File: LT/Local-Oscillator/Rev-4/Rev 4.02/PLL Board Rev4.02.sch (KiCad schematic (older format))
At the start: 69 parts, among them J1 Conn_01x02_Male, J13 Conn_01x02_Male, J14 Conn_01x02_Male, J15 Conn_01x02_Male, J16 Conn_01x02_Male, J17 Conn_01x02_Male, J18 Conn_Coaxial, J2 Conn_Coaxial, J20 Conn_01x02_Male, J3 Conn_Coaxial, J4 Conn_01x04_Male, J5 Conn_01x02_Male, J7 Conn_01x02_Male, J8 Conn_01x02_Male, Q1 2N5486 JFET, Q2 2N5486 JFET, U1 LMX231X, U2 L7808

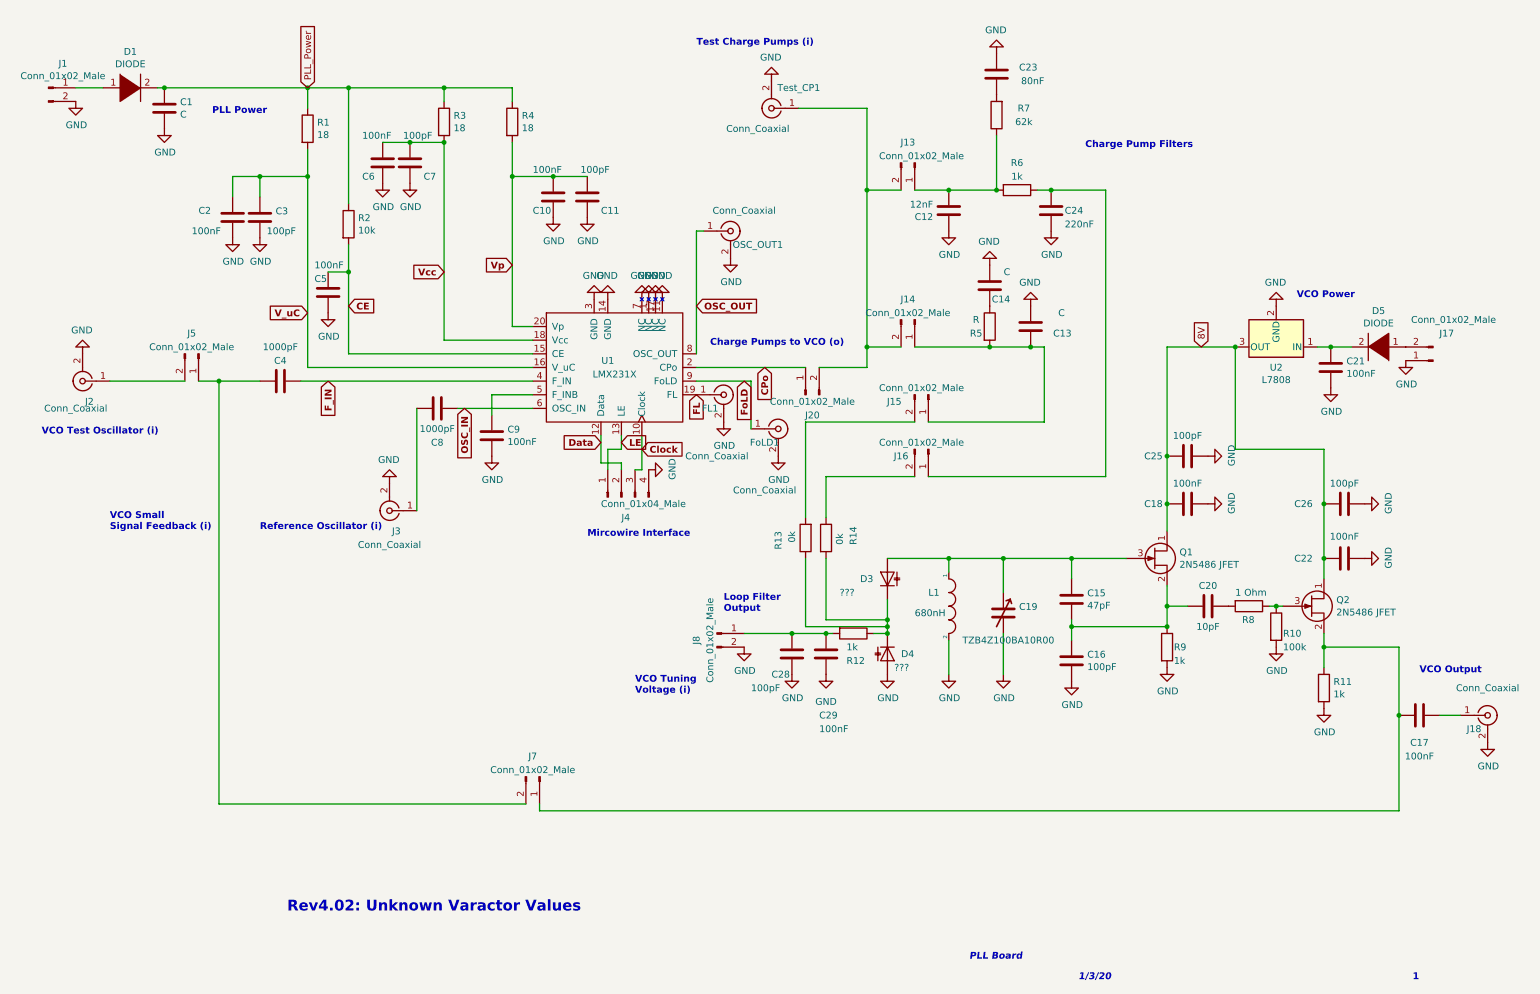
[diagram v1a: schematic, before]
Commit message: Finished PLL Revisions on KiCad
The KiCad files for the PLL have been uploaded to github and the integration to the "Real Resistor" symbol has begun
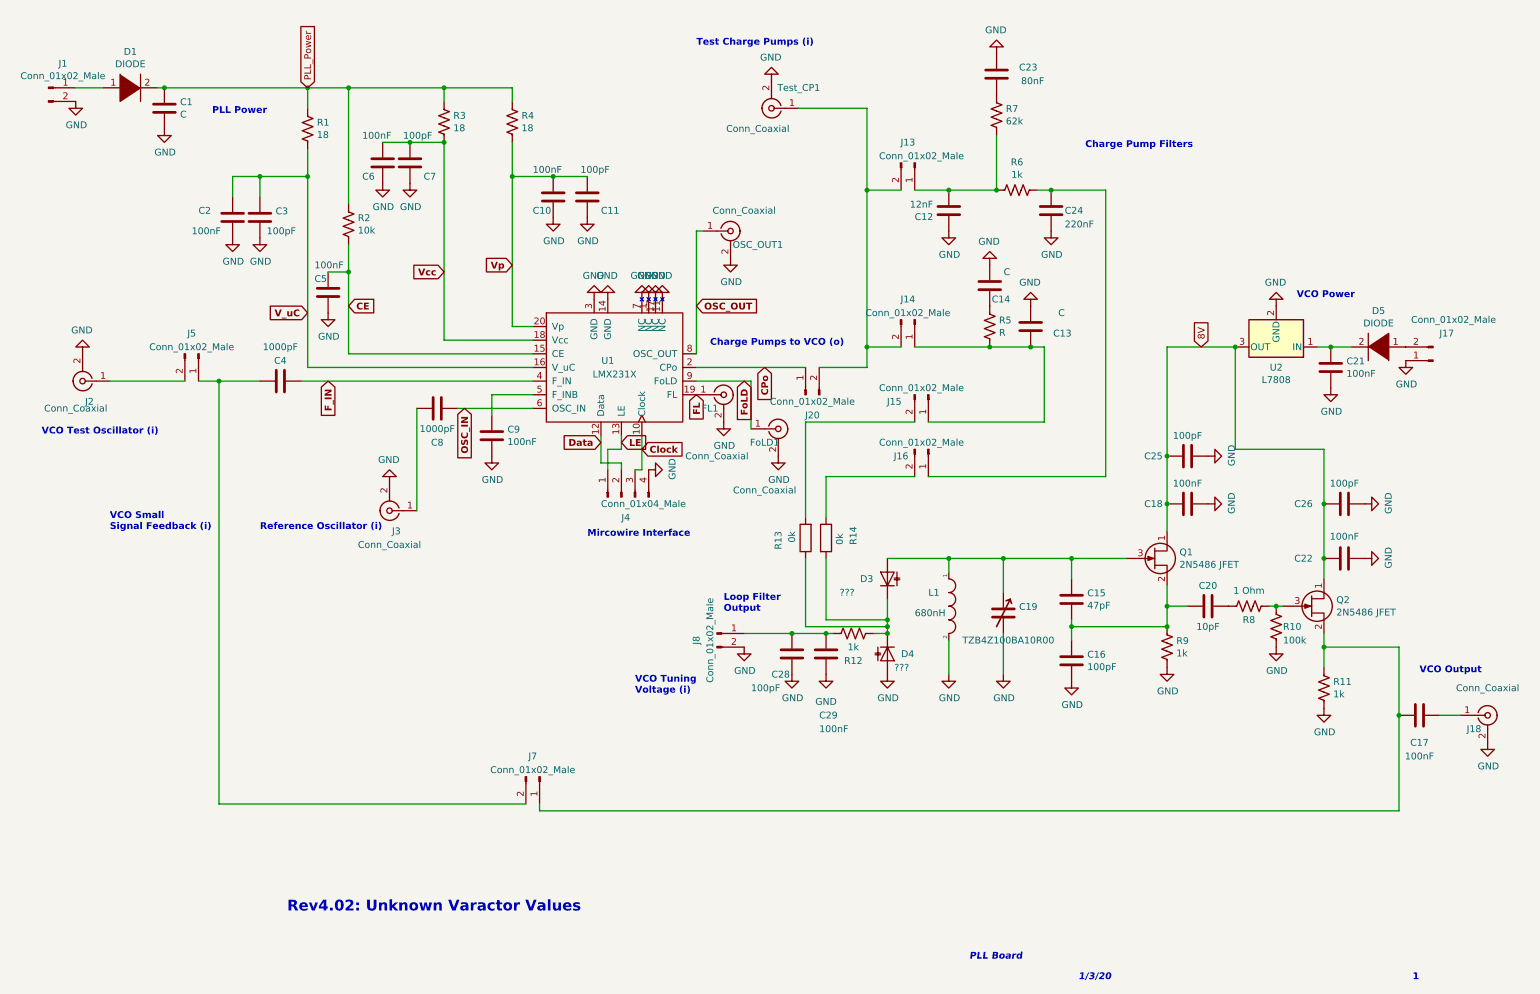
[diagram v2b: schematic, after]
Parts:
- removed R1, R3, R4: 18, Resistor_SMD:R_0805_2012Metric_Pad1.15x1.40mm_HandSolder, symbol PLL-Board-Rev4.02-rescue:R-Device-Complete-PLL-Board-Rev4-rescue-PLL-Board-Rev4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
- removed R10: 100k, Resistor_SMD:R_0805_2012Metric_Pad1.15x1.40mm_HandSolder, symbol PLL-Board-Rev4.02-rescue:R-Device-Complete-PLL-Board-Rev4-rescue-PLL-Board-Rev4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
- removed R11, R12, R6, R9: 1k, Resistor_SMD:R_0805_2012Metric_Pad1.15x1.40mm_HandSolder, symbol PLL-Board-Rev4.02-rescue:R-Device-Complete-PLL-Board-Rev4-rescue-PLL-Board-Rev4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
- removed R2: 10k, Resistor_SMD:R_0805_2012Metric_Pad1.15x1.40mm_HandSolder, symbol PLL-Board-Rev4.02-rescue:R-Device-Complete-PLL-Board-Rev4-rescue-PLL-Board-Rev4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
- removed R5: R, Resistor_SMD:R_0805_2012Metric_Pad1.15x1.40mm_HandSolder, symbol PLL-Board-Rev4.02-rescue:R-Device-Complete-PLL-Board-Rev4-rescue-PLL-Board-Rev4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
- removed R7: 62k, Resistor_SMD:R_0805_2012Metric_Pad1.15x1.40mm_HandSolder, symbol PLL-Board-Rev4.02-rescue:R-Device-Complete-PLL-Board-Rev4-rescue-PLL-Board-Rev4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
- removed R8: 1 Ohm, Resistor_SMD:R_0805_2012Metric_Pad1.15x1.40mm_HandSolder, symbol PLL-Board-Rev4.02-rescue:R-Device-Complete-PLL-Board-Rev4-rescue-PLL-Board-Rev4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
- added R1, R3, R4: 18, Resistor_SMD:R_0805_2012Metric_Pad1.15x1.40mm_HandSolder, symbol Device:R
- added R10: 100k, Resistor_SMD:R_0805_2012Metric_Pad1.15x1.40mm_HandSolder, symbol Device:R
- added R11, R12, R6, R9: 1k, Resistor_SMD:R_0805_2012Metric_Pad1.15x1.40mm_HandSolder, symbol Device:R
- added R2: 10k, Resistor_SMD:R_0805_2012Metric_Pad1.15x1.40mm_HandSolder, symbol Device:R
- added R5: R, Resistor_SMD:R_0805_2012Metric_Pad1.15x1.40mm_HandSolder, symbol Device:R
- added R7: 62k, Resistor_SMD:R_0805_2012Metric_Pad1.15x1.40mm_HandSolder, symbol Device:R
- added R8: 1 Ohm, Resistor_SMD:R_0805_2012Metric_Pad1.15x1.40mm_HandSolder, symbol Device:R
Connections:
- net CE: now also R2.2
- net GND: now also R10.2, R11.2, R9.2
- net PLL_Power: now also R1.1, R2.1, R3.1, R4.1
- net V_uC: now also R1.2
- net Vcc: now also R3.2
- net Vp: now also R4.2
- net at C15.1, C16.2, C20.1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: now also R9.1
- net at D3.1 (K), D4.1 (K), R13.1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: now also R12.1
- net at C20.2: now also R8.2
- net at Q2.3 (G): now also R10.1, R8.1
- net at C17.1, J7.1 (Pin_1), Q2.2 (S): now also R11.1
- net at C13.1, J14.1 (Pin_1), J15.1 (Pin_1): now also R5.2
- net at C12.2, J13.1 (Pin_1): now also R6.2, R7.2
- net at C24.1, J16.1 (Pin_1): now also R6.1
- net at C28.2, C29.2, J8.1 (Pin_1): now also R12.2
- net at C14.1: now also R5.1
- net at C23.1: now also R7.1
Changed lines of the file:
@@
 	0    -1   -1   0
 $EndComp
-$Comp
-L PLL-Board-Rev4.02-rescue:R-Device-Complete-PLL-Board-Rev4-rescue-PLL-Board-Rev4.01-rescue R1
-U 1 1 5C6B70C1
-P 2500 1400
-F 0 "R1" H 2570 1446 50  0000 L CNN
-F 1 "18" H 2570 1355 50  0000 L CNN
-F 2 "Resistor_SMD:R_0805_2012Metric_Pad1.15x1.40mm_HandSolder" V 2430 1400 50  0001 C CNN
-F 3 "~" H 2500 1400 50  0001 C CNN
-	1    2500 1400
-	1    0    0    -1
-$EndComp
-$Comp
-L PLL-Board-Rev4.02-rescue:R-Device-Complete-PLL-Board-Rev4-rescue-PLL-Board-Rev4.01-rescue R3
-U 1 1 5C6B724B
-P 3500 1350
-F 0 "R3" H 3570 1396 50  0000 L CNN
-F 1 "18" H 3570 1305 50  0000 L CNN
-F 2 "Resistor_SMD:R_0805_2012Metric_Pad1.15x1.40mm_HandSolder" V 3430 1350 50  0001 C CNN
-F 3 "~" H 3500 1350 50  0001 C CNN
-	1    3500 1350
-	1    0    0    -1
-$EndComp
-$Comp
-L PLL-Board-Rev4.02-rescue:R-Device-Complete-PLL-Board-Rev4-rescue-PLL-Board-Rev4.01-rescue R4
-U 1 1 5C6B7281
-P 4000 1350
-F 0 "R4" H 4070 1396 50  0000 L CNN
-F 1 "18" H 4070 1305 50  0000 L CNN
-F 2 "Resistor_SMD:R_0805_2012Metric_Pad1.15x1.40mm_HandSolder" V 3930 1350 50  0001 C CNN
-F 3 "~" H 4000 1350 50  0001 C CNN
-	1    4000 1350
-	1    0    0    -1
-$EndComp
 Wire Wire Line
 	2450 3250 4150 3250
-$Comp
-L PLL-Board-Rev4.02-rescue:R-Device-Complete-PLL-Board-Rev4-rescue-PLL-Board-Rev4.01-rescue R2
-U 1 1 5C6B86E4
-P 2800 2100
-F 0 "R2" H 2870 2146 50  0000 L CNN
-F 1 "10k" H 2870 2055 50  0000 L CNN
-F 2 "Resistor_SMD:R_0805_2012Metric_Pad1.15x1.40mm_HandSolder" V 2730 2100 50  0001 C CNN
-F 3 "~" H 2800 2100 50  0001 C CNN
-	1    2800 2100
-	1    0    0    -1
-$EndComp
 Wire Wire Line
 	2500 1100 2500 1250
@@
 Wire Wire Line
 	3500 2950 4150 2950
-Connection ~ 3500 1500
 $Comp
 L power:GND #PWR08
@@
 $EndComp
 $Comp
-L PLL-Board-Rev4.02-rescue:R-Device-Complete-PLL-Board-Rev4-rescue-PLL-Board-Rev4.01-rescue R9
-U 1 1 5C802100
-P 8800 5200
-F 0 "R9" H 8850 5200 50  0000 L CNN
-F 1 "1k" H 8850 5100 50  0000 L CNN
-F 2 "Resistor_SMD:R_0805_2012Metric_Pad1.15x1.40mm_HandSolder" V 8730 5200 50  0001 C CNN
-F 3 "~" H 8800 5200 50  0001 C CNN
-	1    8800 5200
-	1    0    0    -1
-$EndComp
-$Comp
 L power:GND #PWR031
 U 1 1 5C8038C6
@@
 	8100 5050 8100 5150
 $Comp
-L PLL-Board-Rev4.02-rescue:R-Device-Complete-PLL-Board-Rev4-rescue-PLL-Board-Rev4.01-rescue R10
-U 1 1 5C809914
-P 9600 5050
-F 0 "R10" H 9650 5000 50  0000 L CNN
-F 1 "100k" H 9650 4900 50  0000 L CNN
-F 2 "Resistor_SMD:R_0805_2012Metric_Pad1.15x1.40mm_HandSolder" V 9530 5050 50  0001 C CNN
-F 3 "~" H 9600 5050 50  0001 C CNN
-	1    9600 5050
-	1    0    0    -1
-$EndComp
-$Comp
 L power:GND #PWR033
 U 1 1 5C809EFF
@@
 F 3 "" H 9600 5200 50  0001 C CNN
 	1    9600 5200
-	1    0    0    -1
-$EndComp
-$Comp
-L PLL-Board-Rev4.02-rescue:R-Device-Complete-PLL-Board-Rev4-rescue-PLL-Board-Rev4.01-rescue R11
-U 1 1 5C80AB36
-P 9950 5500
-F 0 "R11" H 10020 5546 50  0000 L CNN
-F 1 "1k" H 10020 5455 50  0000 L CNN
-F 2 "Resistor_SMD:R_0805_2012Metric_Pad1.15x1.40mm_HandSolder" V 9880 5500 50  0001 C CNN
-F 3 "~" H 9950 5500 50  0001 C CNN
-	1    9950 5500
 	1    0    0    -1
 $EndComp
@@
 Wire Wire Line
 	6750 5000 6750 5050
-Connection ~ 8800 5050
 Wire Wire Line
 	8100 4700 8100 4550
@@
 	7200 1850 7550 1850
 Connection ~ 7200 1850
-$Comp
-L PLL-Board-Rev4.02-rescue:R-Device-Complete-PLL-Board-Rev4-rescue-PLL-Board-Rev4.01-rescue R6
-U 1 1 5C863D30
-P 7700 1850
-F 0 "R6" V 7500 1850 50  0000 C CNN
-F 1 "1k" V 7600 1850 50  0000 C CNN
-F 2 "Resistor_SMD:R_0805_2012Metric_Pad1.15x1.40mm_HandSolder" V 7630 1850 50  0001 C CNN
-F 3 "~" H 7700 1850 50  0001 C CNN
-	1    7700 1850
-	0    1    1    0
-$EndComp
 $Comp
 L power:GND #PWR0103
@@
 	7800 3000 7900 3000
 $Comp
-L PLL-Board-Rev4.02-rescue:R-Device-Complete-PLL-Board-Rev4-rescue-PLL-Board-Rev4.01-rescue R5
-U 1 1 5C8FC8A8
-P 7500 2850
-F 0 "R5" H 7400 2800 50  0000 C CNN
-F 1 "R" H 7400 2900 50  0000 C CNN
-F 2 "Resistor_SMD:R_0805_2012Metric_Pad1.15x1.40mm_HandSolder" V 7430 2850 50  0001 C CNN
-F 3 "~" H 7500 2850 50  0001 C CNN
-	1    7500 2850
-	1    0    0    -1
-$EndComp
-$Comp
 L Device:C C14
 U 1 1 5C8FCBE4
@@
 	-1   0    0    1
 $EndComp
-Wire Wire Line
-	6950 3000 7500 3000
-Connection ~ 7500 3000
-Wire Wire Line
-	7500 3000 7800 3000
 Wire Wire Line
 	10500 6400 4200 6400
@@
 Wire Wire Line
 	8800 4750 8800 4900
-$Comp
-L PLL-Board-Rev4.02-rescue:R-Device-Complete-PLL-Board-Rev4-rescue-PLL-Board-Rev4.01-rescue R8
-U 1 1 5CA66BF5
-P 9400 4900
-F 0 "R8" V 9500 4850 50  0000 L CNN
-F 1 "1 Ohm" V 9300 4800 50  0000 L CNN
-F 2 "Resistor_SMD:R_0805_2012Metric_Pad1.15x1.40mm_HandSolder" V 9330 4900 50  0001 C CNN
-F 3 "~" H 9400 4900 50  0001 C CNN
-	1    9400 4900
-	0    1    1    0
-$EndComp
-Wire Wire Line
-	9550 4900 9600 4900
-Connection ~ 9600 4900
-Wire Wire Line
-	9600 4900 9650 4900
 Connection ~ 8800 4900
 Wire Wire Line
@@
 	-1   0    0    1
 $EndComp
-$Comp
-L PLL-Board-Rev4.02-rescue:R-Device-Complete-PLL-Board-Rev4-rescue-PLL-Board-Rev4.01-rescue R7
-U 1 1 5CA7D1B6
-P 7550 1300
-F 0 "R7" H 7350 1250 50  0000 C CNN
-F 1 "62k" H 7350 1350 50  0000 C CNN
-F 2 "Resistor_SMD:R_0805_2012Metric_Pad1.15x1.40mm_HandSolder" V 7480 1300 50  0001 C CNN
-F 3 "~" H 7550 1300 50  0001 C CNN
-	1    7550 1300
-	-1   0    0    1
-$EndComp
 Wire Wire Line
 	7550 1850 7550 1450
-Connection ~ 7550 1850
 $Comp
 L power:GND #PWR027
@@
 $EndComp
 Connection ~ 9950 4550
-$Comp
-L PLL-Board-Rev4.02-rescue:R-Device-Complete-PLL-Board-Rev4-rescue-PLL-Board-Rev4.01-rescue R12
-U 1 1 5CB9DB4B
-P 6500 5100
-F 0 "R12" V 6700 5050 50  0000 L CNN
-F 1 "1k" V 6600 5050 50  0000 L CNN
-F 2 "Resistor_SMD:R_0805_2012Metric_Pad1.15x1.40mm_HandSolder" V 6430 5100 50  0001 C CNN
-F 3 "~" H 6500 5100 50  0001 C CNN
-	1    6500 5100
-	0    1    1    0
-$EndComp
 Wire Wire Line
 	8800 4900 8950 4900
@@
 Text Notes 2350 7150 0    79   ~ 16
 Rev4.02: Unknown Varactor Values
+$Comp
+L Device:R R1
+U 1 1 5E5BE92F
+P 2500 1400
+F 0 "R1" H 2568 1446 50  0000 L CNN
+F 1 "18" H 2568 1355 50  0000 L CNN
+F 2 "Resistor_SMD:R_0805_2012Metric_Pad1.15x1.40mm_HandSolder" V 2540 1390 50  0001 C CNN
+F 3 "~" H 2500 1400 50  0001 C CNN
+	1    2500 1400
+	1    0    0    -1
+$EndComp
+$Comp
+L Device:R R2
+U 1 1 5E5CF74D
+P 2800 2100
+F 0 "R2" H 2868 2146 50  0000 L CNN
+F 1 "10k" H 2868 2055 50  0000 L CNN
+F 2 "Resistor_SMD:R_0805_2012Metric_Pad1.15x1.40mm_HandSolder" V 2840 2090 50  0001 C CNN
+F 3 "~" H 2800 2100 50  0001 C CNN
+	1    2800 2100
+	1    0    0    -1
+$EndComp
+$Comp
+L Device:R R3
+U 1 1 5E5D8387
+P 3500 1350
+F 0 "R3" H 3568 1396 50  0000 L CNN
+F 1 "18" H 3568 1305 50  0000 L CNN
+F 2 "Resistor_SMD:R_0805_2012Metric_Pad1.15x1.40mm_HandSolder" V 3540 1340 50  0001 C CNN
+F 3 "~" H 3500 1350 50  0001 C CNN
+	1    3500 1350
+	1    0    0    -1
+$EndComp
+Connection ~ 3500 1500
+$Comp
+L Device:R R4
+U 1 1 5E602E93
+P 4000 1350
+F 0 "R4" H 4068 1396 50  0000 L CNN
+F 1 "18" H 4068 1305 50  0000 L CNN
+F 2 "Resistor_SMD:R_0805_2012Metric_Pad1.15x1.40mm_HandSolder" V 4040 1340 50  0001 C CNN
+F 3 "~" H 4000 1350 50  0001 C CNN
+	1    4000 1350
+	1    0    0    -1
+$EndComp
+$Comp
+L Device:R R7
+U 1 1 5E60981A
+P 7550 1300
+F 0 "R7" H 7618 1346 50  0000 L CNN
+F 1 "62k" H 7618 1255 50  0000 L CNN
+F 2 "Resistor_SMD:R_0805_2012Metric_Pad1.15x1.40mm_HandSolder" V 7590 1290 50  0001 C CNN
+F 3 "~" H 7550 1300 50  0001 C CNN
+	1    7550 1300
+	1    0    0    -1
+$EndComp
+$Comp
+L Device:R R6
+U 1 1 5E61214C
+P 7700 1850
+F 0 "R6" V 7495 1850 50  0000 C CNN
+F 1 "1k" V 7586 1850 50  0000 C CNN
+F 2 "Resistor_SMD:R_0805_2012Metric_Pad1.15x1.40mm_HandSolder" V 7740 1840 50  0001 C CNN
+F 3 "~" H 7700 1850 50  0001 C CNN
+	1    7700 1850
+	0    1    1    0
+$EndComp
+Connection ~ 7550 1850
+Wire Wire Line
+	6950 3000 7500 3000
+$Comp
+L Device:R R5
+U 1 1 5E62005C
+P 7500 2850
+F 0 "R5" H 7568 2896 50  0000 L CNN
+F 1 "R" H 7568 2805 50  0000 L CNN
+F 2 "Resistor_SMD:R_0805_2012Metric_Pad1.15x1.40mm_HandSolder" V 7540 2840 50  0001 C CNN
+F 3 "~" H 7500 2850 50  0001 C CNN
+	1    7500 2850
+	1    0    0    -1
+$EndComp
+Connection ~ 7500 3000
+Wire Wire Line
+	7500 3000 7800 3000
+$Comp
+L Device:R R12
+U 1 1 5E6214BA
+P 6500 5100
+F 0 "R12" V 6700 5100 50  0000 C CNN
+F 1 "1k" V 6600 5100 50  0000 C CNN
+F 2 "Resistor_SMD:R_0805_2012Metric_Pad1.15x1.40mm_HandSolder" V 6540 5090 50  0001 C CNN
+F 3 "~" H 6500 5100 50  0001 C CNN
+	1    6500 5100
+	0    1    1    0
+$EndComp
+$Comp
+L Device:R R9
+U 1 1 5E62803C
+P 8800 5200
+F 0 "R9" H 8868 5246 50  0000 L CNN
+F 1 "1k" H 8868 5155 50  0000 L CNN
+F 2 "Resistor_SMD:R_0805_2012Metric_Pad1.15x1.40mm_HandSolder" V 8840 5190 50  0001 C CNN
+F 3 "~" H 8800 5200 50  0001 C CNN
+	1    8800 5200
+	1    0    0    -1
+$EndComp
+Connection ~ 8800 5050
+$Comp
+L Device:R R8
+U 1 1 5E62E4C4
+P 9400 4900
+F 0 "R8" V 9500 4900 50  0000 C CNN
+F 1 "1 Ohm" V 9286 4900 50  0000 C CNN
+F 2 "Resistor_SMD:R_0805_2012Metric_Pad1.15x1.40mm_HandSolder" V 9440 4890 50  0001 C CNN
+F 3 "~" H 9400 4900 50  0001 C CNN
+	1    9400 4900
+	0    1    1    0
+$EndComp
+$Comp
+L Device:R R10
+U 1 1 5E63424F
+P 9600 5050
+F 0 "R10" H 9650 5050 50  0000 L CNN
+F 1 "100k" H 9650 4950 50  0000 L CNN
+F 2 "Resistor_SMD:R_0805_2012Metric_Pad1.15x1.40mm_HandSolder" V 9640 5040 50  0001 C CNN
+F 3 "~" H 9600 5050 50  0001 C CNN
+	1    9600 5050
+	1    0    0    -1
+$EndComp
+Wire Wire Line
+	9550 4900 9600 4900
+Connection ~ 9600 4900
+Wire Wire Line
+	9600 4900 9650 4900
+$Comp
+L Device:R R11
+U 1 1 5E63AEDD
+P 9950 5500
+F 0 "R11" H 10018 5546 50  0000 L CNN
+F 1 "1k" H 10018 5455 50  0000 L CNN
+F 2 "Resistor_SMD:R_0805_2012Metric_Pad1.15x1.40mm_HandSolder" V 9990 5490 50  0001 C CNN
+F 3 "~" H 9950 5500 50  0001 C CNN
+	1    9950 5500
+	1    0    0    -1
+$EndComp
 $EndSCHEMATC
